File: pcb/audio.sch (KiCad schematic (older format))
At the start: 0 parts

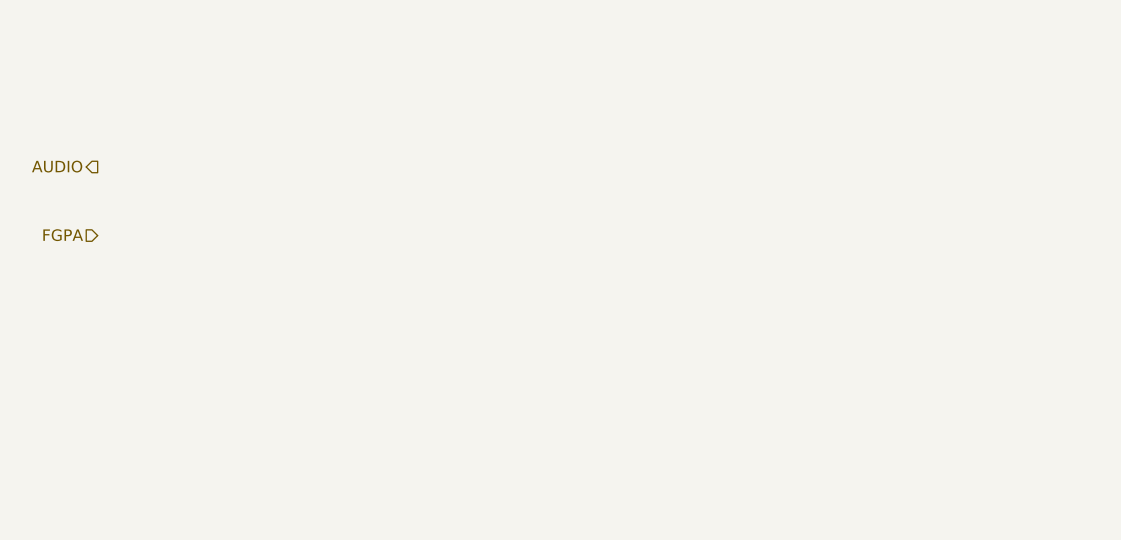
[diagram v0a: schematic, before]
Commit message: buffer section finished, audio moved to expansion connector
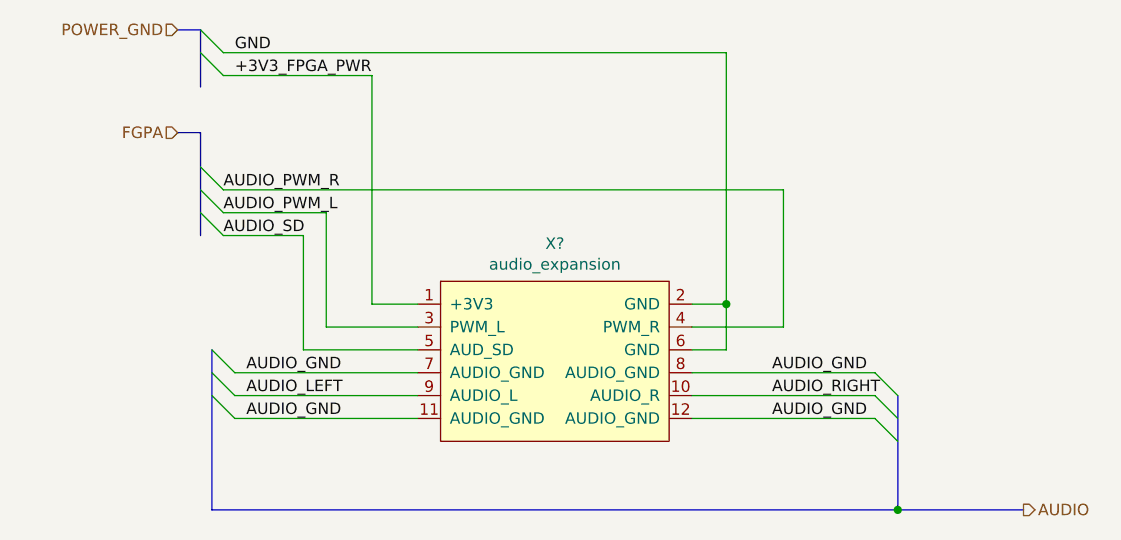
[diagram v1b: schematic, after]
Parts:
- added X?: audio_expansion, symbol WM1200:audio_expansion
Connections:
- new net +3V3_FPGA_PWR: X?.1 (+3V3)
- new net AUDIO_GND: X?.11 (AUDIO_GND), X?.12 (AUDIO_GND), X?.7 (AUDIO_GND), X?.8 (AUDIO_GND)
- new net AUDIO_LEFT: X?.9 (AUDIO_L)
- new net AUDIO_PWM_L: X?.3 (PWM_L)
- new net AUDIO_PWM_R: X?.4 (PWM_R)
- new net AUDIO_RIGHT: X?.10 (AUDIO_R)
- new net AUDIO_SD: X?.5 (AUD_SD)
- new net GND: X?.2 (GND), X?.6 (GND)
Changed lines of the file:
@@
 Comment4 ""
 $EndDescr
-Text HLabel 1000 1500 0    50   Output ~ 0
+Text HLabel 5050 3000 2    50   Output ~ 0
 AUDIO
-Text HLabel 1000 1800 0    50   Input ~ 0
+Text HLabel 1350 1350 0    50   Input ~ 0
 FGPA
+Wire Bus Line
+	1350 1350 1450 1350
+Entry Wire Line
+	1450 1600 1550 1700
+Entry Wire Line
+	1450 1500 1550 1600
+Wire Wire Line
+	1550 1700 2000 1700
+Text Label 1550 1700 0    50   ~ 0
+AUDIO_PWM_L
+Text Label 1550 1600 0    50   ~ 0
+AUDIO_PWM_R
+Text HLabel 1350 900  0    50   Input ~ 0
+POWER_GND
+$Comp
+L WM1200:audio_expansion X?
+U 1 1 5EB21AAB
+P 3000 2700
+F 0 "X?" H 3000 3565 50  0000 C CNN
+F 1 "audio_expansion" H 3000 3474 50  0000 C CNN
+F 2 "" H 2400 2950 50  0001 C CNN
+F 3 "" H 2400 2950 50  0001 C CNN
+	1    3000 2700
+	1    0    0    -1
+$EndComp
+Wire Bus Line
+	1500 3000 4500 3000
+Connection ~ 4500 3000
+Wire Bus Line
+	4500 3000 5050 3000
+Wire Wire Line
+	4000 1600 4000 2200
+Wire Wire Line
+	4000 2200 3600 2200
+Wire Wire Line
+	1550 1600 4000 1600
+Wire Wire Line
+	2000 1700 2000 2200
+Wire Wire Line
+	2000 2200 2400 2200
+Entry Wire Line
+	1500 2300 1600 2400
+Entry Wire Line
+	1500 2400 1600 2500
+Entry Wire Line
+	1500 2500 1600 2600
+Entry Wire Line
+	4400 2400 4500 2500
+Entry Wire Line
+	4400 2500 4500 2600
+Entry Wire Line
+	4400 2600 4500 2700
+Wire Wire Line
+	1600 2400 2400 2400
+Wire Wire Line
+	2400 2500 1600 2500
+Wire Wire Line
+	1600 2600 2400 2600
+Wire Wire Line
+	3600 2400 4400 2400
+Wire Wire Line
+	4400 2500 3600 2500
+Wire Wire Line
+	3600 2600 4400 2600
+Entry Wire Line
+	1450 1700 1550 1800
+Wire Wire Line
+	1550 1800 1900 1800
+Wire Wire Line
+	1900 1800 1900 2300
+Wire Wire Line
+	1900 2300 2400 2300
+Text Label 1550 1800 0    50   ~ 0
+AUDIO_SD
+Wire Bus Line
+	1350 900  1450 900
+Entry Wire Line
+	1450 900  1550 1000
+Entry Wire Line
+	1450 1000 1550 1100
+Wire Wire Line
+	1550 1100 2200 1100
+Wire Wire Line
+	2200 1100 2200 2100
+Wire Wire Line
+	2200 2100 2400 2100
+Wire Wire Line
+	3750 2100 3600 2100
+Wire Wire Line
+	3750 2100 3750 2300
+Wire Wire Line
+	3750 2300 3600 2300
+Connection ~ 3750 2100
+Wire Wire Line
+	1550 1000 3750 1000
+Wire Wire Line
+	3750 1000 3750 2100
+Text Label 1600 1100 0    50   ~ 0
++3V3_FPGA_PWR
+Text Label 1600 1000 0    50   ~ 0
+GND
+Wire Bus Line
+	1450 900  1450 1150
+Wire Bus Line
+	1500 2300 1500 3000
+Wire Bus Line
+	4500 2500 4500 3000
+Wire Bus Line
+	1450 1350 1450 1800
+Text Label 1650 2400 0    50   ~ 0
+AUDIO_GND
+Text Label 1650 2600 0    50   ~ 0
+AUDIO_GND
+Text Label 3950 2600 0    50   ~ 0
+AUDIO_GND
+Text Label 3950 2400 0    50   ~ 0
+AUDIO_GND
+Text Label 1650 2500 0    50   ~ 0
+AUDIO_LEFT
+Text Label 3950 2500 0    50   ~ 0
+AUDIO_RIGHT
 $EndSCHEMATC
